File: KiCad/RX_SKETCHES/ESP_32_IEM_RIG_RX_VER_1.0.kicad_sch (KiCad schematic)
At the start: 0 parts

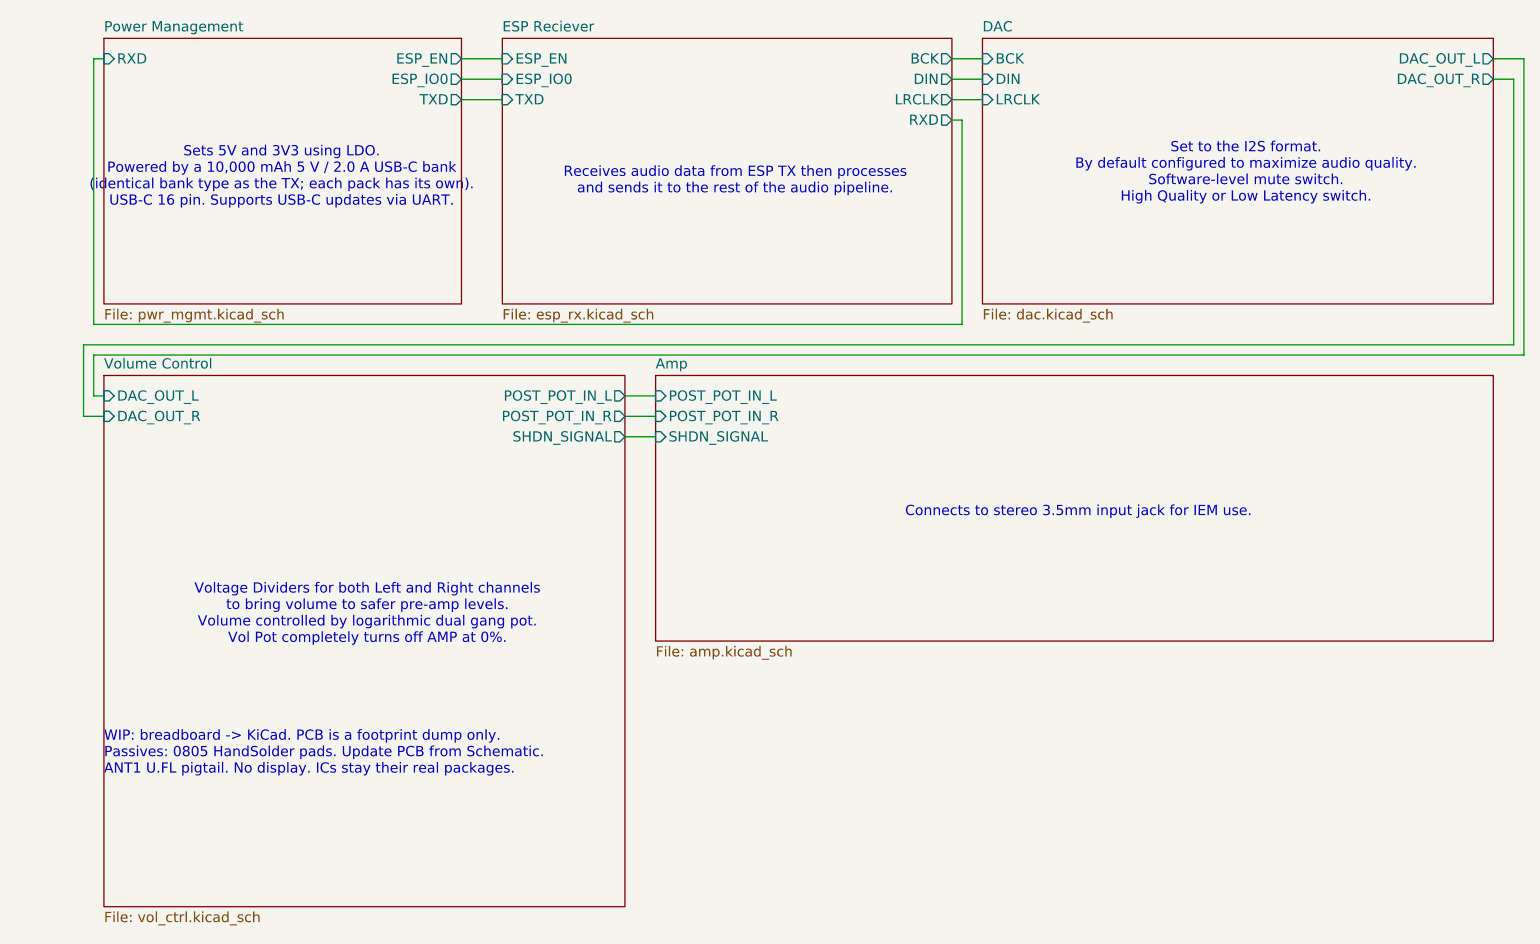
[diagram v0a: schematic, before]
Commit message: WIP: RX schematic review — restore DAC/amp, fix ESP nets, log revisions.
Restore dac/amp from main after rotate damage, rename I2S net to DOUT,
mark amp gain Rs DNP, and record change/rationale in docs/hardware_revisions.org.

Co-authored-by: Cursor <cursoragent@cursor.com>
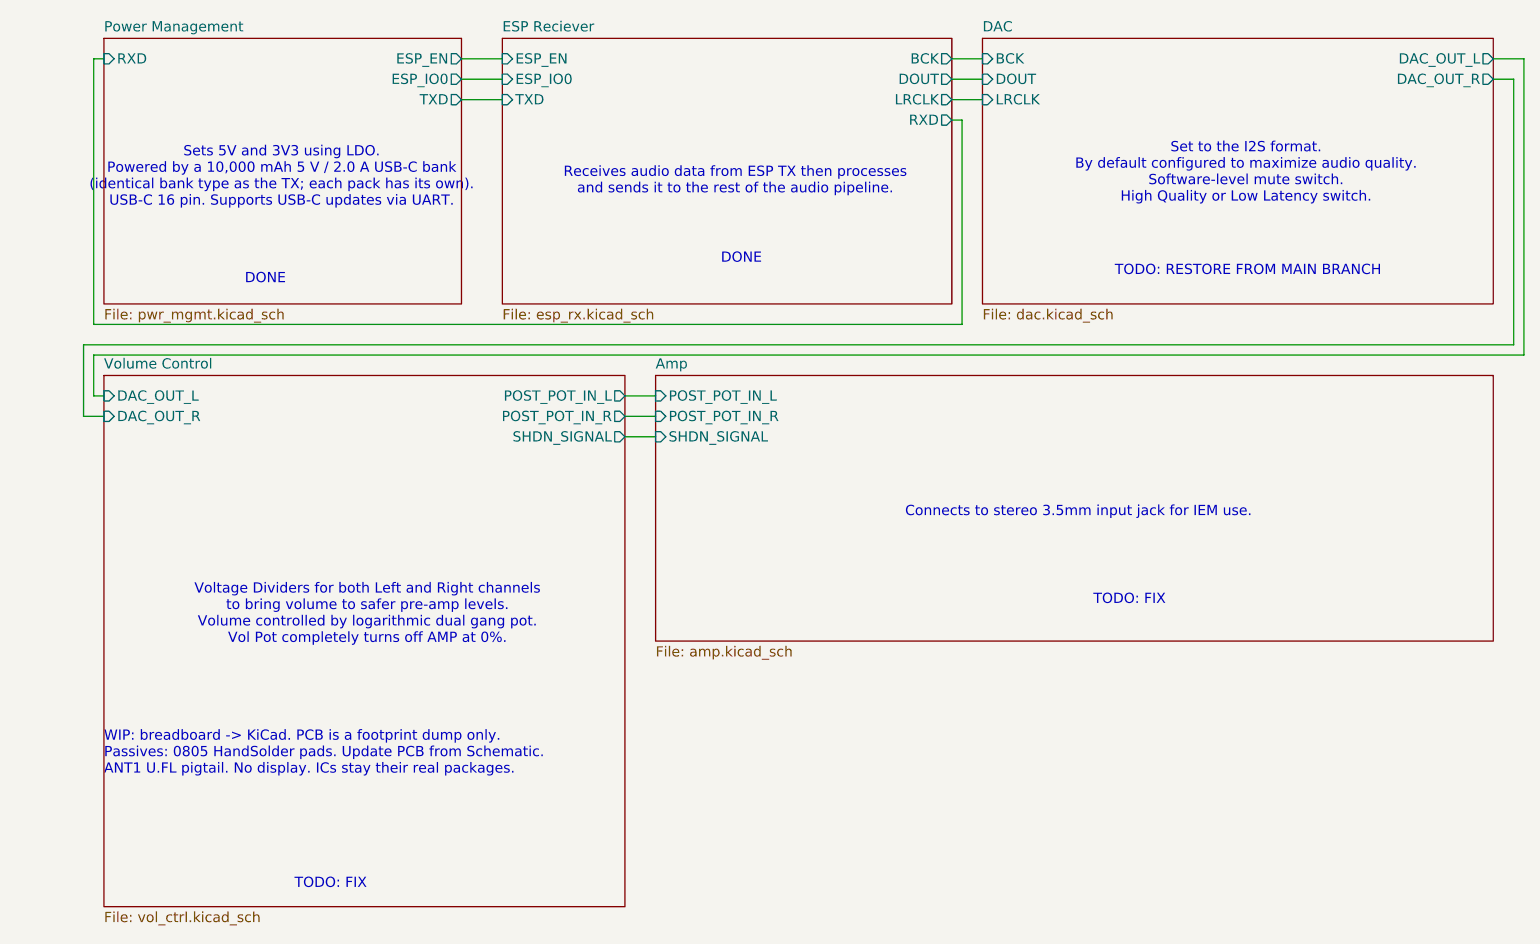
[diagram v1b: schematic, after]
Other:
- sheet DAC ports: added DOUT; removed DIN
- sheet ESP Reciever ports: added DOUT; removed DIN
- note added: "DONE"
- note added: "TODO: FIX"
- note added: "TODO: RESTORE FROM MAIN BRANCH"
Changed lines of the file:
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@@
 		(comment 4 "Supports updates over USB-C using UART.")
 	)
+	(text "DONE"
+		(exclude_from_sim no)
+		(at 37.846 51.562 0)
+		(effects
+			(font
+				(size 1.27 1.27)
+			)
+		)
+	)
+	(text "DONE"
+		(exclude_from_sim no)
+		(at 97.028 49.022 0)
+		(effects
+			(font
+				(size 1.27 1.27)
+			)
+		)
+	)
 	(text "Voltage Dividers for both Left and Right channels\nto bring volume to safer pre-amp levels. \nVolume controlled by logarithmic dual gang pot.\nVol Pot completely turns off AMP at 0%.\n"
 		(exclude_from_sim no)
@@
 		)
 	)
+	(text "TODO: RESTORE FROM MAIN BRANCH"
+		(exclude_from_sim no)
+		(at 160.02 50.546 0)
+		(effects
+			(font
+				(size 1.27 1.27)
+			)
+		)
+	)
+	(text "TODO: FIX"
+		(exclude_from_sim no)
+		(at 145.288 91.44 0)
+		(effects
+			(font
+				(size 1.27 1.27)
+			)
+		)
+	)
+	(text "TODO: FIX"
+		(exclude_from_sim no)
+		(at 45.974 126.746 0)
+		(effects
+			(font
+				(size 1.27 1.27)
+			)
+		)
+	)
 	(text "Receives audio data from ESP TX then processes \nand sends it to the rest of the audio pipeline."
 		(exclude_from_sim no)
@@
 		)
 	)
+	(text "WIP: breadboard -> KiCad. PCB is a footprint dump only.\nPassives: 0805 HandSolder pads. Update PCB from Schematic.\nANT1 U.FL pigtail. No display. ICs stay their real packages."
+		(exclude_from_sim no)
+		(at 17.78 110.49 0)
+		(effects
+			(font
+				(size 1.27 1.27)
+			)
+			(justify left)
+		)
+	)
 	(text "Sets 5V and 3V3 using LDO.\nPowered by a 10,000 mAh 5 V / 2.0 A USB-C bank\n(identical bank type as the TX; each pack has its own).\nUSB-C 16 pin. Supports USB-C updates via UART."
 		(exclude_from_sim no)
@@
 	(wire
 		(pts
+			(xy 123.19 26.67) (xy 127 26.67)
+		)
+		(stroke
+			(width 0)
+			(type default)
+		)
+	)
+	(wire
+		(pts
 			(xy 15.24 59.69) (xy 15.24 68.58)
 		)
@@
 	(wire
 		(pts
-			(xy 123.19 26.67) (xy 127 26.67)
-		)
-		(stroke
-			(width 0)
-			(type default)
-		)
-	)
-	(wire
-		(pts
 			(xy 16.51 60.96) (xy 16.51 66.04)
 		)
@@
 			(width 0)
 			(type default)
-		)
-	)
-	(text "WIP: breadboard -> KiCad. PCB is a footprint dump only.\nPassives: 0805 HandSolder pads. Update PCB from Schematic.\nANT1 U.FL pigtail. No display. ICs stay their real packages."
-		(exclude_from_sim no)
-		(at 17.78 110.49 0)
-		(effects
-			(font
-				(size 1.27 1.27)
-			)
-			(justify left)
 		)
 	)
@@
 			)
 		)
-		(pin "DIN" output
-			(at 123.19 26.67 0)
-			(effects
-				(font
-					(size 1.27 1.27)
-				)
-				(justify right)
-			)
-		)
 		(pin "LRCLK" output
 			(at 123.19 29.21 0)
@@
 		(pin "RXD" output
 			(at 123.19 31.75 0)
+			(effects
+				(font
+					(size 1.27 1.27)
+				)
+				(justify right)
+			)
+		)
+		(pin "DOUT" output
+			(at 123.19 26.67 0)
 			(effects
 				(font
@@
 			)
 		)
-		(pin "DIN" input
-			(at 127 26.67 180)
-			(effects
-				(font
-					(size 1.27 1.27)
-				)
-				(justify left)
-			)
-		)
 		(pin "LRCLK" input
 			(at 127 29.21 180)
@@
 			)
 		)
+		(pin "DOUT" input
+			(at 127 26.67 180)
+			(effects
+				(font
+					(size 1.27 1.27)
+				)
+				(justify left)
+			)
+		)

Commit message: RX: finish layout, retune gain/coupling, move ESD clamp to unswitched VBUS
Board now passes DRC with zero unconnected items and zero schematic-parity
issues. Remaining 16 violations are footprint-inherent (ESP32 module thermal
via array at 0.2 mm drill, USB-C NPTH-to-pad spacing) and are documented
rather than routed around.

Analog changes, with the reasoning captured in README.org and
docs/hardware_revisions.org so the numbers can be re-checked:

- Gain network populated at RF 4.7k / RIN 47k (-20 dB) instead of DNP 10k.
  Tames the DAC's 2.1 Vrms into sensitive IEMs, unloads the pot taper, and
  moves the coupling corner out of the audible band.
- Coupling caps C1-C4 0.47uF -> 1uF. Corner 7.2 Hz -> 3.4 Hz, and it halves
  the signal developed across the ceramic at 20 Hz, cutting Class-II
  dielectric distortion where it actually occurs.
- D1's third TVS channel moved off the switched +5V rail onto VBUS_RAW. The
  clamp has to sit on the connector pin that is exposed to a finger; behind
  the power switch it went open exactly when the board is most handled.
- SW3 soft mute: XSMT_SEL moved to the throw that puts mute on the south
  slide position. All three switches now follow one rule -- the open throw
  is the safe default (off / quality filter / muted).
- PCM5102 mode pins no longer float: FLT and XSMT get 100k pulldowns, DEMP
  and FMT strap to GND.
- C28 and the four mounting holes added to the schematic to clear parity
  errors against parts that only existed on the PCB.

Also adds a .gitignore so the 24 MB editor .history/ directory and ESP-IDF
build output stop showing up as untracked.

Co-authored-by: Cursor <cursoragent@cursor.com>
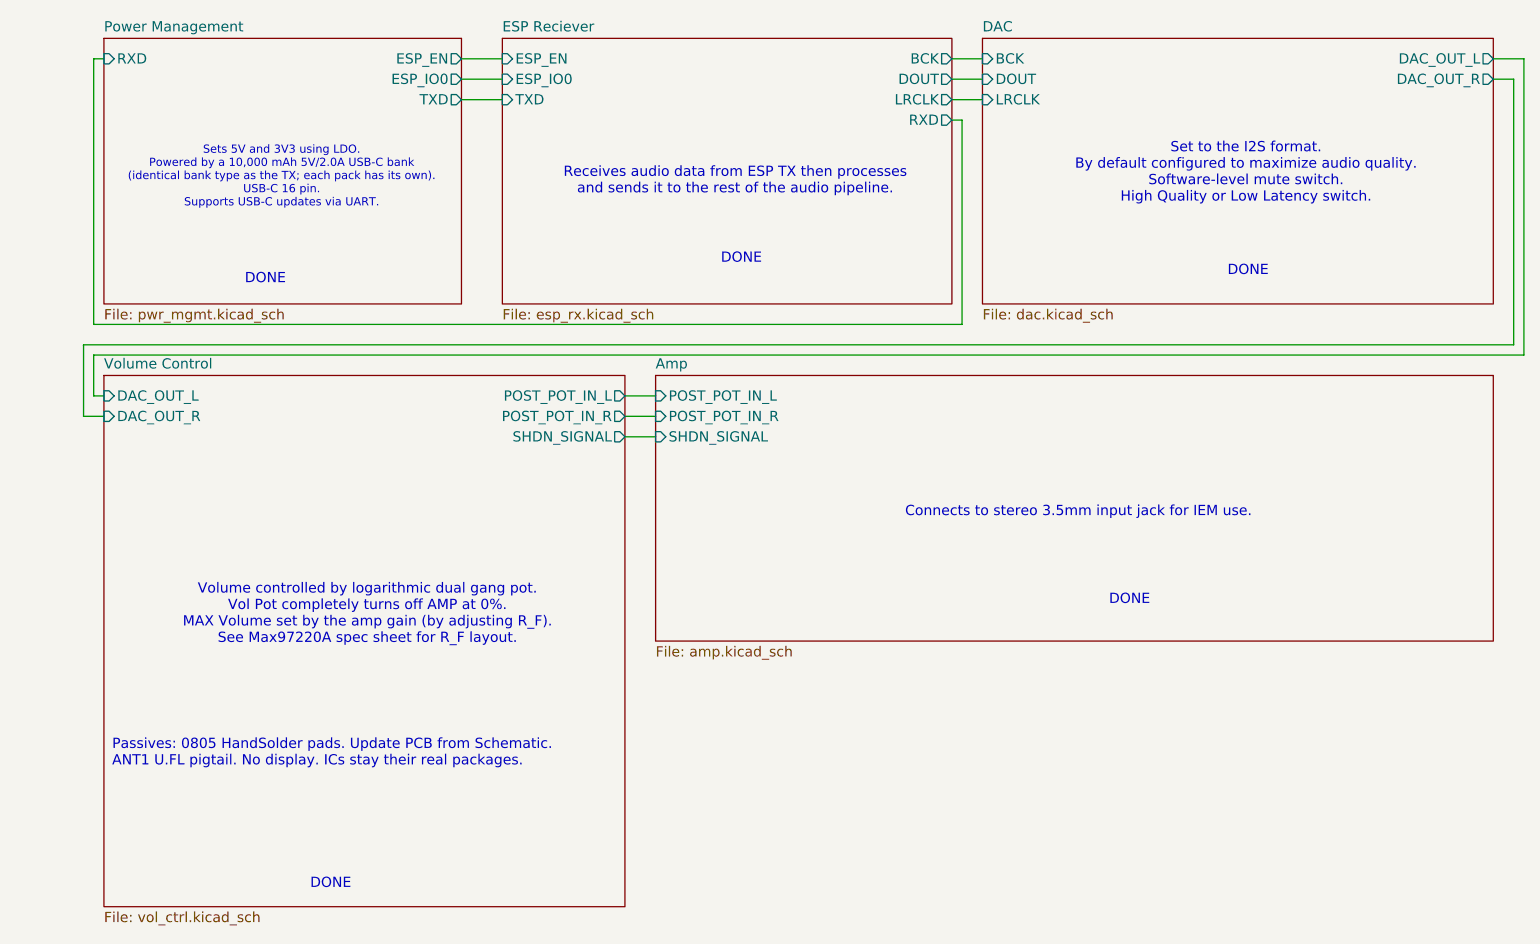
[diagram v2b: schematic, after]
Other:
- note added: "Passives: 0805 HandSolder pads. Update PCB from Schematic. ANT1 U.FL pigtail. No display. ICs stay their real packages."
- note added: "Sets 5V and 3V3 using LDO. Powered by a 10,000 mAh 5V/2.0A USB-C bank (identical bank type as the TX; each pack has its own). USB-C 16 pin. Supports USB-C updates via UART."
- note added: "Volume controlled by logarithmic dual gang pot. Vol Pot completely turns off AMP at 0%. MAX Volume set by the amp gain (by adjusting R_F). See Max97220A spec sheet for R_F layout."
- note removed: "Sets 5V and 3V3 using LDO. Powered by a 10,000 mAh 5 V / 2.0 A USB-C bank (identical bank type as the TX; each pack has its own). USB-C 16 pin. Supports USB-C updates via UART."
- note removed: "TODO: FIX"
- note removed: "TODO: RESTORE FROM MAIN BRANCH"
- note removed: "Voltage Dividers for both Left and Right channels to bring volume to safer pre-amp levels. Volume controlled by logarithmic dual gang pot. Vol Pot completely turns off AMP at 0%."
- note removed: "WIP: breadboard -> KiCad. PCB is a footprint dump only. Passives: 0805 HandSolder pads. Update PCB from Schematic. ANT1 U.FL pigtail. No display. ICs stay their real packages."
- title: ESP32 Wireless IEM Rig Reciever -> ESP32U- WROOM Wireless IEM Rig Reciever
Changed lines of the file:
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@@
 	(paper "A5")
 	(title_block
-		(title "ESP32 Wireless IEM Rig Reciever")
+		(title "ESP32U- WROOM Wireless IEM Rig Reciever")
 		(date "2026-08-04")
 		(rev "1.0.0")
@@
 		)
 	)
-	(text "Voltage Dividers for both Left and Right channels\nto bring volume to safer pre-amp levels. \nVolume controlled by logarithmic dual gang pot.\nVol Pot completely turns off AMP at 0%.\n"
+	(text "Volume controlled by logarithmic dual gang pot.\nVol Pot completely turns off AMP at 0%.\nMAX Volume set by the amp gain (by adjusting R_F). \nSee Max97220A spec sheet for R_F layout."
 		(exclude_from_sim no)
 		(at 50.546 93.218 0)
@@
 		)
 	)
-	(text "TODO: RESTORE FROM MAIN BRANCH"
+	(text "DONE"
 		(exclude_from_sim no)
 		(at 160.02 50.546 0)
@@
 		)
 	)
-	(text "TODO: FIX"
+	(text "DONE"
 		(exclude_from_sim no)
 		(at 145.288 91.44 0)
@@
 		)
 	)
-	(text "TODO: FIX"
+	(text "DONE"
 		(exclude_from_sim no)
 		(at 45.974 126.746 0)
@@
 		)
 	)
-	(text "WIP: breadboard -> KiCad. PCB is a footprint dump only.\nPassives: 0805 HandSolder pads. Update PCB from Schematic.\nANT1 U.FL pigtail. No display. ICs stay their real packages."
+	(text "Passives: 0805 HandSolder pads. Update PCB from Schematic.\nANT1 U.FL pigtail. No display. ICs stay their real packages."
 		(exclude_from_sim no)
-		(at 17.78 110.49 0)
+		(at 18.796 110.49 0)
 		(effects
 			(font
@@
 		)
 	)
-	(text "Sets 5V and 3V3 using LDO.\nPowered by a 10,000 mAh 5 V / 2.0 A USB-C bank\n(identical bank type as the TX; each pack has its own).\nUSB-C 16 pin. Supports USB-C updates via UART."
+	(text "Sets 5V and 3V3 using LDO.\nPowered by a 10,000 mAh 5V/2.0A USB-C bank\n(identical bank type as the TX; each pack has its own).\nUSB-C 16 pin. \nSupports USB-C updates via UART."
 		(exclude_from_sim no)
 		(at 39.878 38.862 0)
 		(effects
 			(font
-				(size 1.27 1.27)
+				(size 1.016 1.016)
 			)
 		)
